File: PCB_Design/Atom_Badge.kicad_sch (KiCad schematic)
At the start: 23 parts

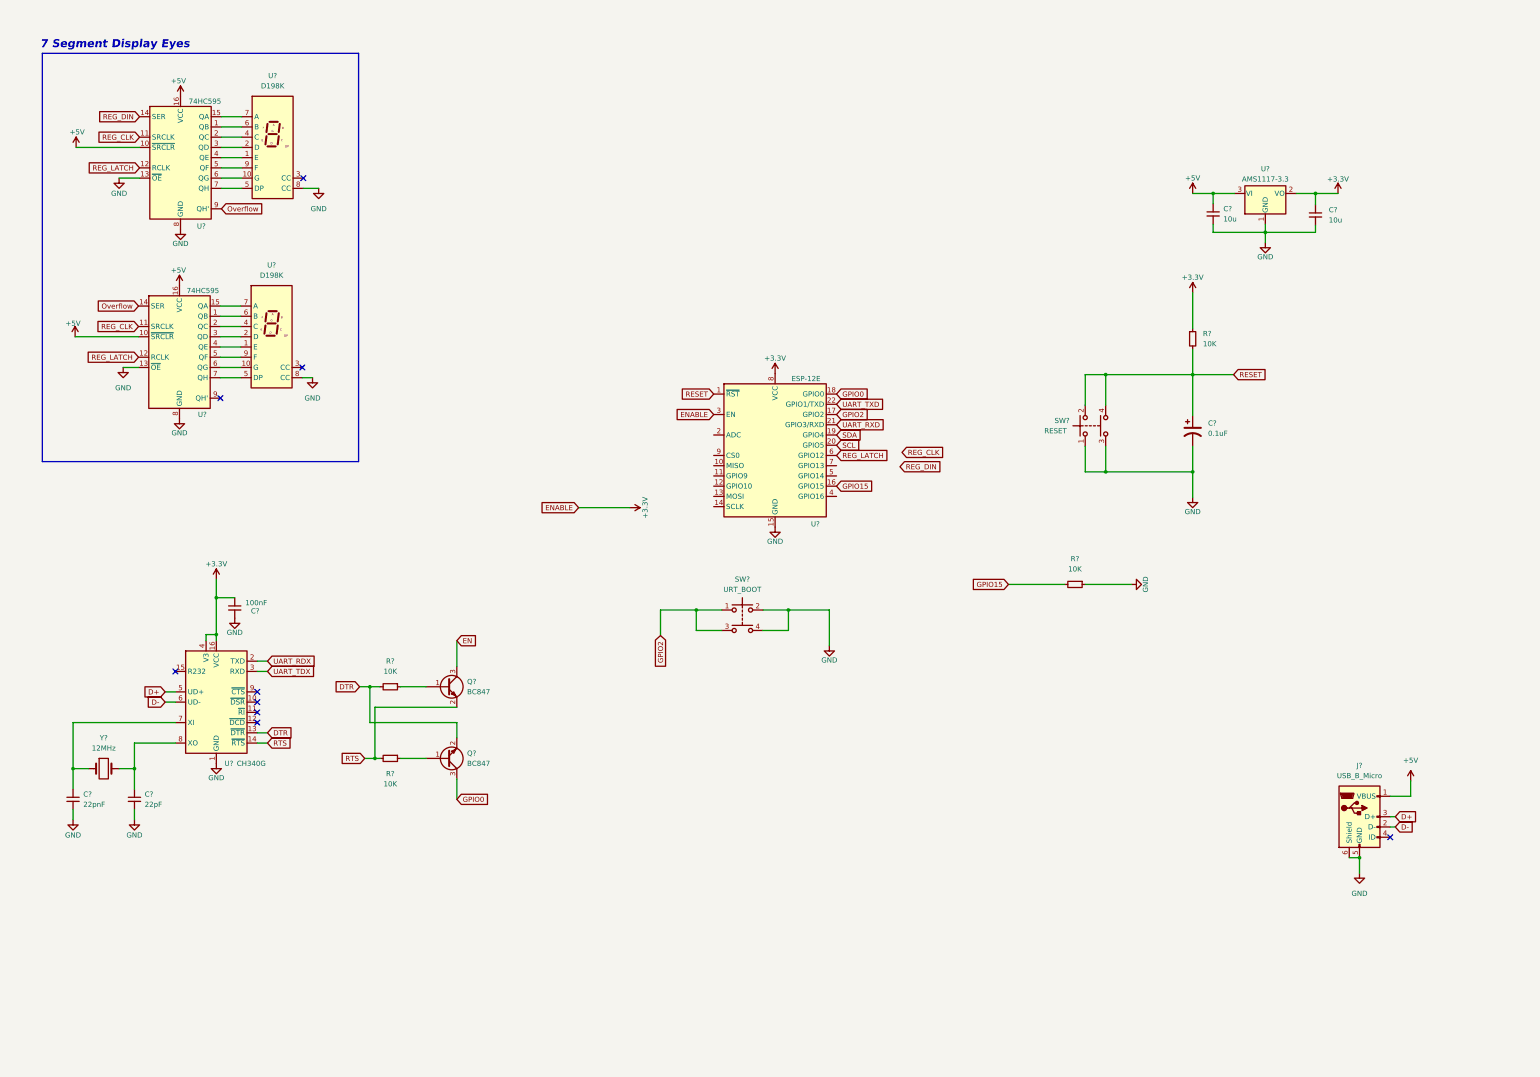
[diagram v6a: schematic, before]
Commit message: Added LEDs and OLED conn
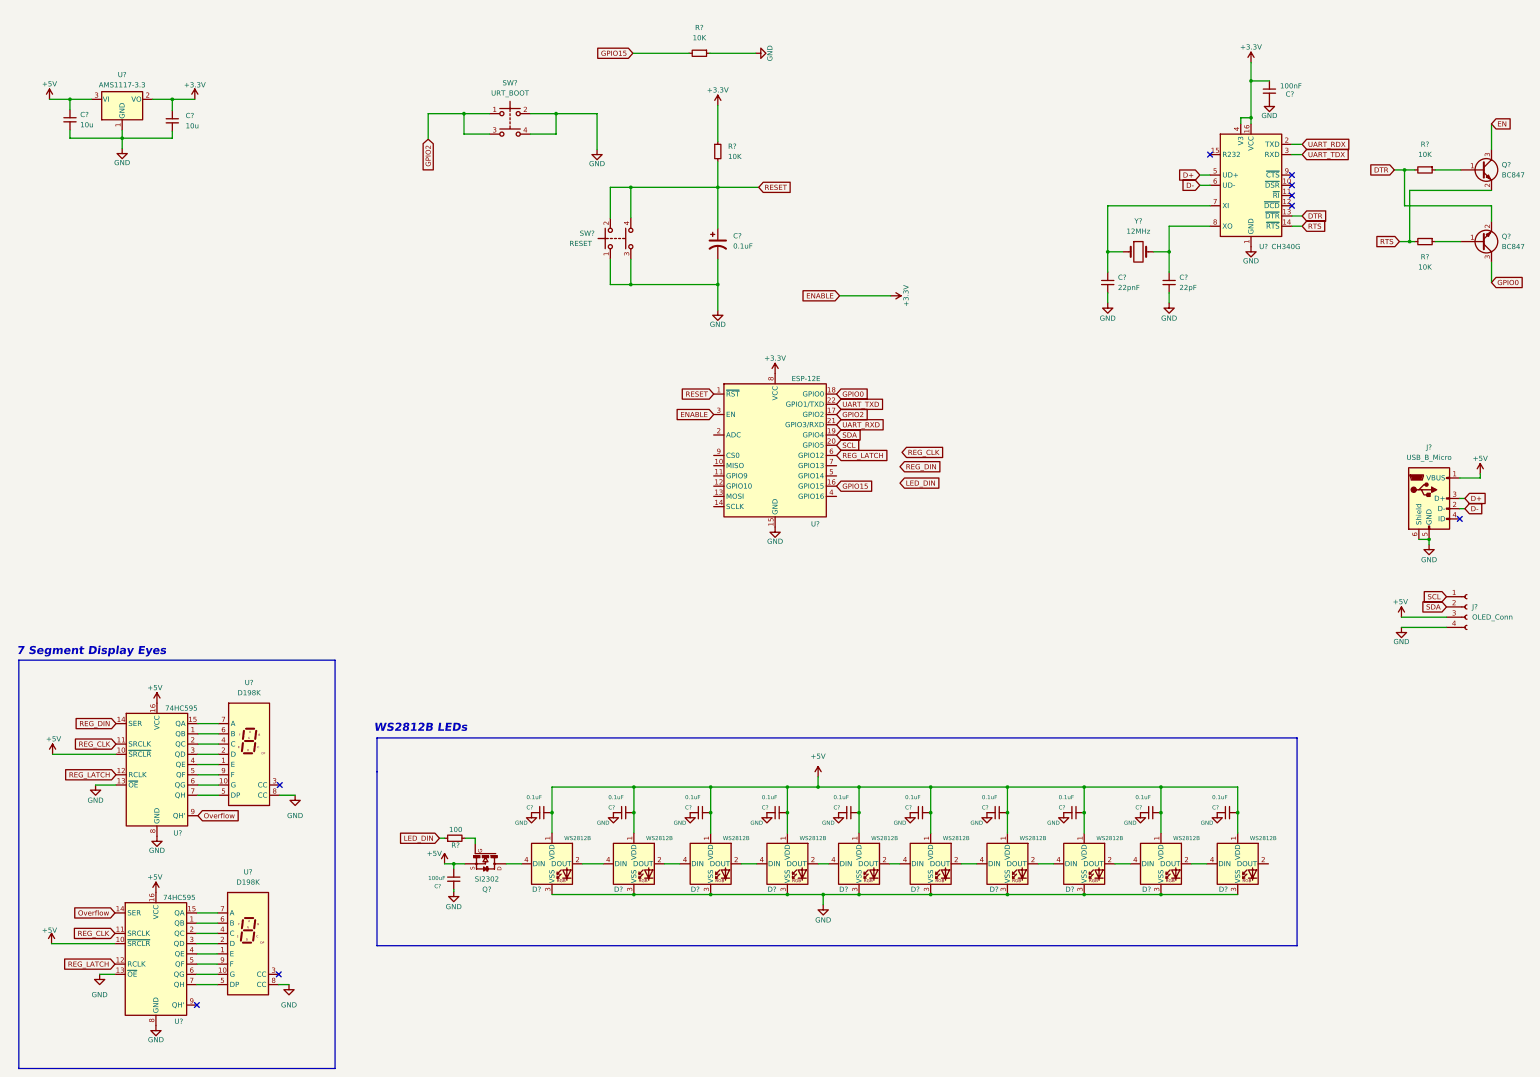
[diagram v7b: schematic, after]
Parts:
- added C? (x10): 0.1uF, Capacitor_SMD:C_1206_3216Metric_Pad1.33x1.80mm_HandSolder, symbol Device:C_Small
- added C?: 100uF, Capacitor_SMD:C_1206_3216Metric_Pad1.33x1.80mm_HandSolder, symbol Device:C_Small
- added D? (x10): WS2812B, LED_SMD:LED_WS2812B_PLCC4_5.0x5.0mm_P3.2mm, symbol LED:WS2812B
- added J?: OLED_Conn, symbol Connector:Conn_01x04_Female
- added Q?: SI2302, Package_TO_SOT_SMD:SOT-23, symbol SI2302:SI2302
- added R?: 100, Resistor_SMD:R_1206_3216Metric_Pad1.30x1.75mm_HandSolder, symbol Device:R_Small
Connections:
- net +5V: now also C?.1, C?.1, C?.1, C?.1, C?.1, C?.1, C?.1, C?.1, C?.1, C?.1, C?.1, D?.1 (VDD), D?.1 (VDD), D?.1 (VDD), D?.1 (VDD), D?.1 (VDD), D?.1 (VDD), D?.1 (VDD), D?.1 (VDD), D?.1 (VDD), D?.1 (VDD), J?.3 (Pin_3), Q?.2
- net GND: now also C?.2, C?.2, C?.2, C?.2, C?.2, C?.2, C?.2, C?.2, C?.2, C?.2, C?.2, D?.3 (VSS), D?.3 (VSS), D?.3 (VSS), D?.3 (VSS), D?.3 (VSS), D?.3 (VSS), D?.3 (VSS), D?.3 (VSS), D?.3 (VSS), D?.3 (VSS), J?.4 (Pin_4)
- net SCL: now also J?.1 (Pin_1)
- net SDA: now also J?.2 (Pin_2)
- new net: D?.2 (DOUT), D?.4 (DIN) (x9)
- new net: D?.4 (DIN), Q?.3
- new net: Q?.1, R?.2
- new net LED_DIN: R?.1
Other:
- note added: "WS2812B LEDs"
- moved on the sheet: C?, J?, Q?, R?, SW?, U?, Y?
